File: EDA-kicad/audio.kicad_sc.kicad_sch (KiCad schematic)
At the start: 6 parts, among them J1 SJ2-35894B-SMT-TR, U7 CODEC-TLV320AIC3204IRHBR, U8 DAC-TLV320DAC3100IRHBR

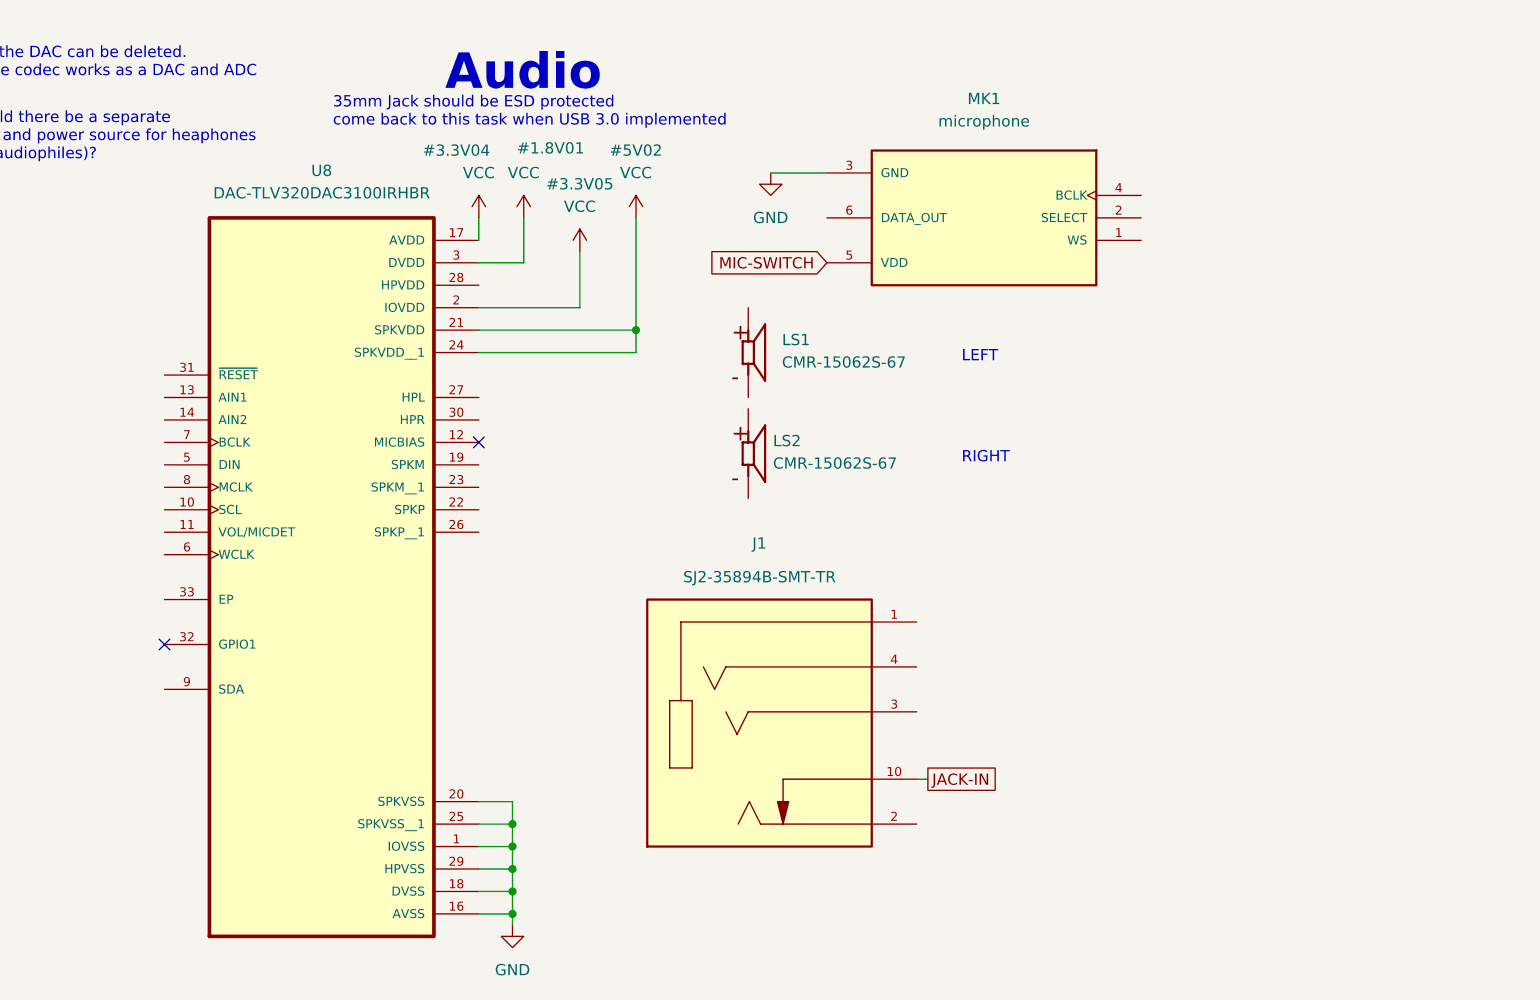
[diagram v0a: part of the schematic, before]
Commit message: add clearance
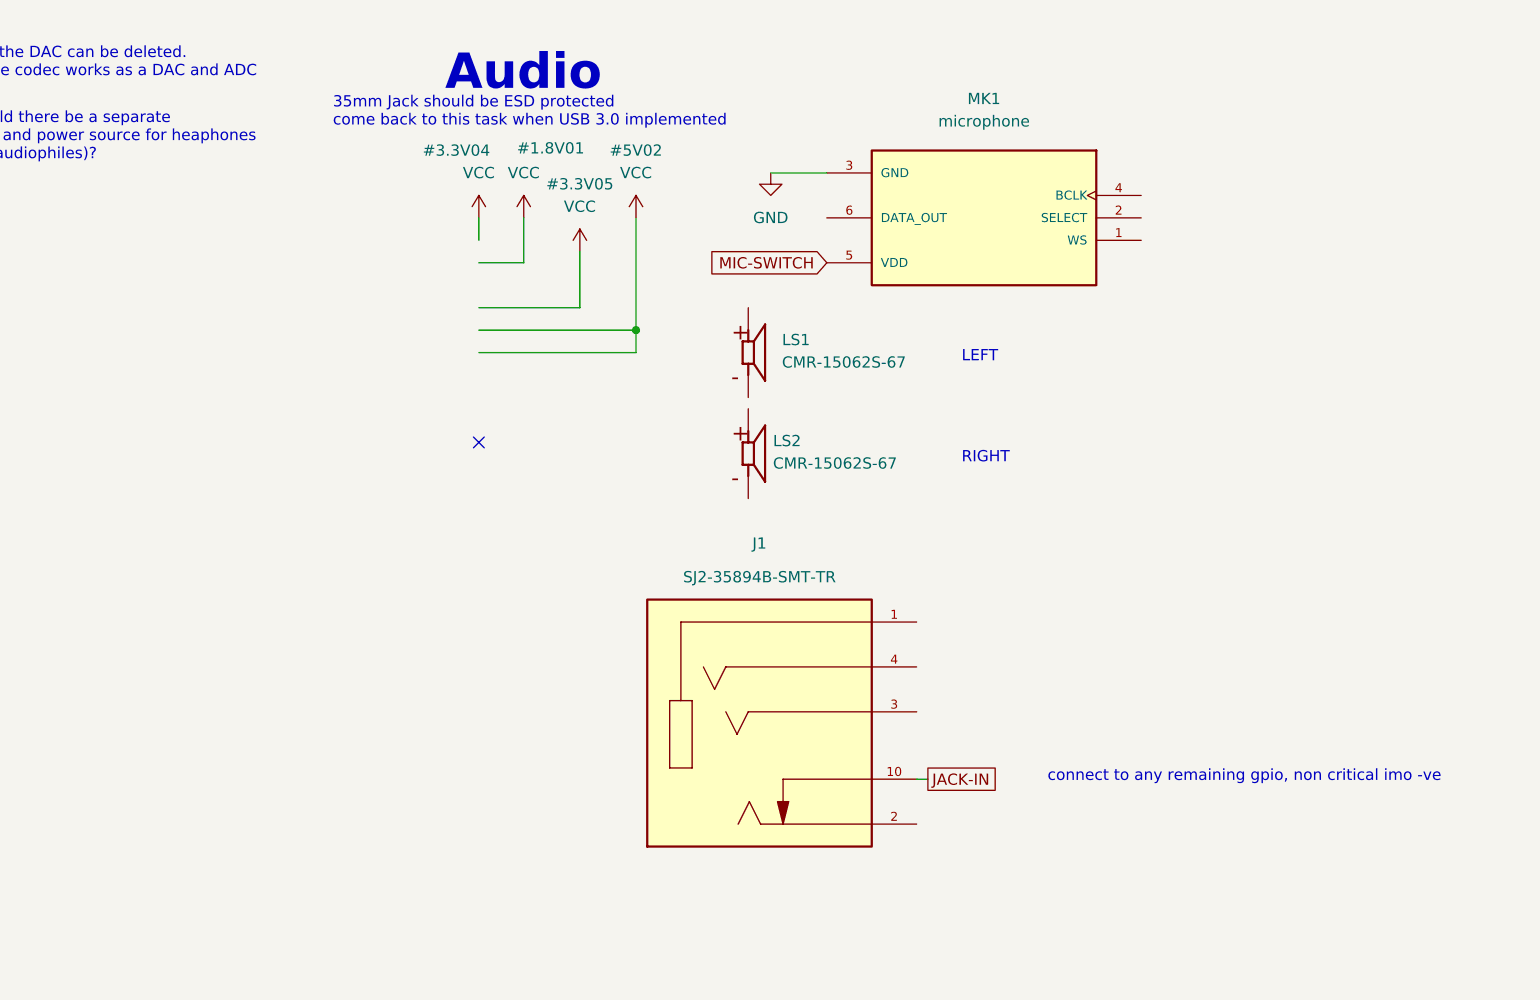
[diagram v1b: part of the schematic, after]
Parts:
- removed U8: DAC-TLV320DAC3100IRHBR, SPIRIT-footprints:DAC-IC_ADS125H01IRHBT, symbol SPIRIT-components:DAC-TLV320DAC3100IRHBR
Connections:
- no-connect marks 4 -> 3
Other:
- note added: "connect to any remaining gpio, non critical imo -ve"

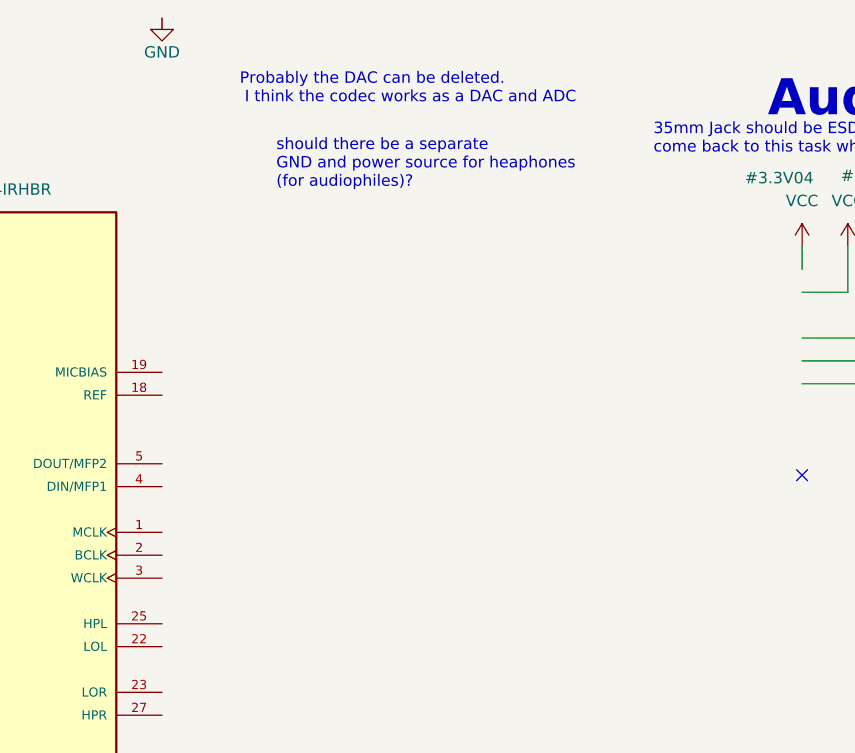
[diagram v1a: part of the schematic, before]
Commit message: connect codec clocks to GPIO and specify alt functions
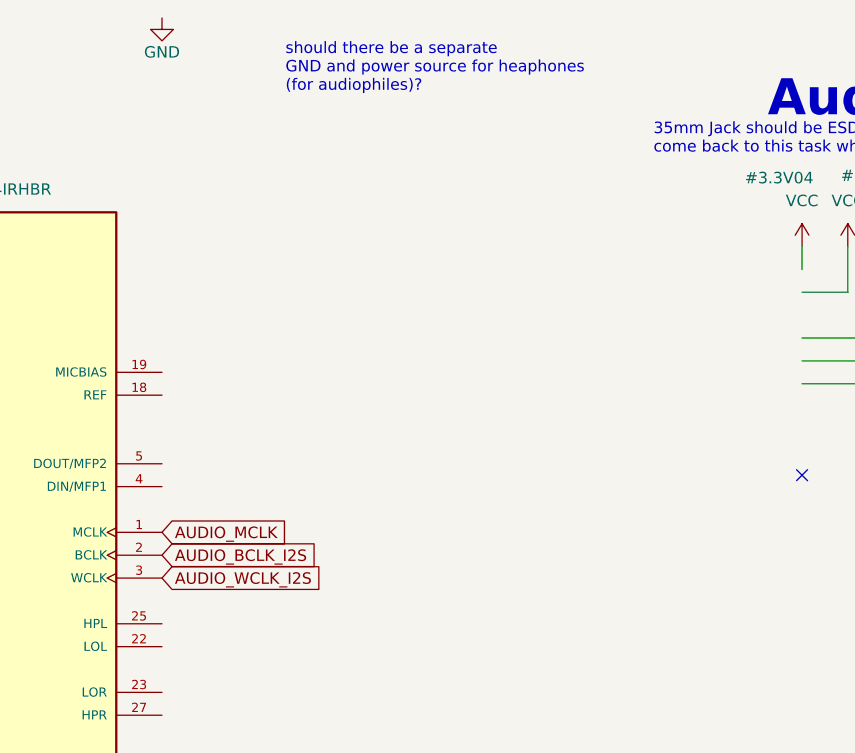
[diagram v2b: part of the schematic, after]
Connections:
- net AUDIO_MCLK: now reaches U7.1 (MCLK)
- net AUDIO_BCLK_I2S: now reaches U7.2 (BCLK)
- net AUDIO_WCLK_I2S: now reaches U7.3 (WCLK)
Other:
- note removed: "Probably the DAC can be deleted. I think the codec works as a DAC and ADC"
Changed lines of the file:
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@@
 	(text "should there be a separate \nGND and power source for heaphones\n(for audiophiles)?"
 		(exclude_from_sim no)
-		(at 118.11 58.42 0)
+		(at 119.126 47.752 0)
 		(effects
 			(font
@@
 		(exclude_from_sim no)
 		(at 231.14 81.28 0)
-		(effects
-			(font
-				(size 1.27 1.27)
-			)
-			(justify left bottom)
-		)
-	)
-	(text "Probably the DAC can be deleted.\n I think the codec works as a DAC and ADC"
-		(exclude_from_sim no)
-		(at 114.046 49.022 0)
 		(effects
 			(font
@@
 		)
 	)
+	(global_label "AUDIO_BCLK_I2S"
+		(shape input)
+		(at 105.41 99.06 0)
+		(fields_autoplaced yes)
+		(effects
+			(font
+				(size 1.27 1.27)
+			)
+			(justify left)
+		)
+		(property "Intersheetrefs" "${INTERSHEET_REFS}"
+			(at 123.8167 99.06 0)
+			(effects
+				(font
+					(size 1.27 1.27)
+				)
+				(justify left)
+				(hide yes)
+			)
+		)
+	)
 	(global_label "CODEC SCL"
 		(shape input)
@@
 				(hide yes)
 			)
+		)
+	)
+	(global_label "AUDIO_WCLK_I2S"
+		(shape input)
+		(at 105.41 101.6 0)
+		(fields_autoplaced yes)
+		(effects
+			(font
+				(size 1.27 1.27)
+			)
+			(justify left)
+		)
+		(property "Intersheetrefs" "${INTERSHEET_REFS}"
+			(at 123.9981 101.6 0)
+			(effects
+				(font
+					(size 1.27 1.27)
+				)
+				(justify left)
+				(hide yes)
+			)
+		)
+	)
+	(global_label "AUDIO_MCLK"
+		(shape input)
+		(at 105.41 96.52 0)
+		(fields_autoplaced yes)
+		(effects
+			(font
+				(size 1.27 1.27)
+			)
+			(justify left)
+		)
+		(property "Intersheetrefs" "${INTERSHEET_REFS}"
+			(at 120.0067 96.52 0)
+			(effects
+				(font
+					(size 1.27 1.27)
+				)
+				(justify left)
+				(hide yes)
+			)

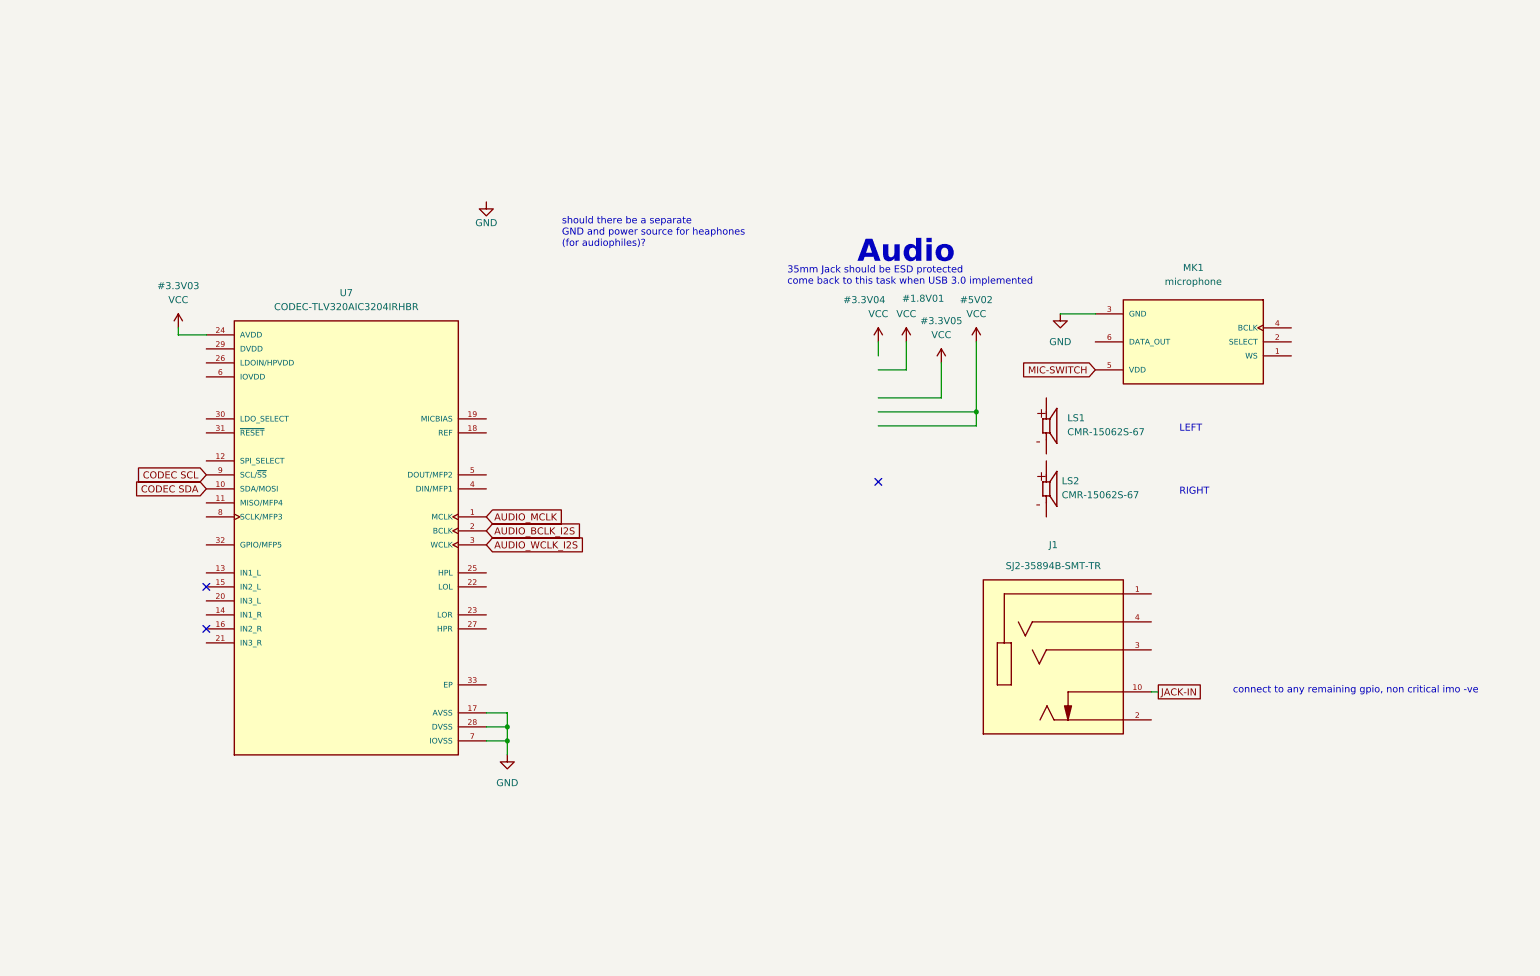
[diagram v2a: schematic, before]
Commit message: microhphone partially connected
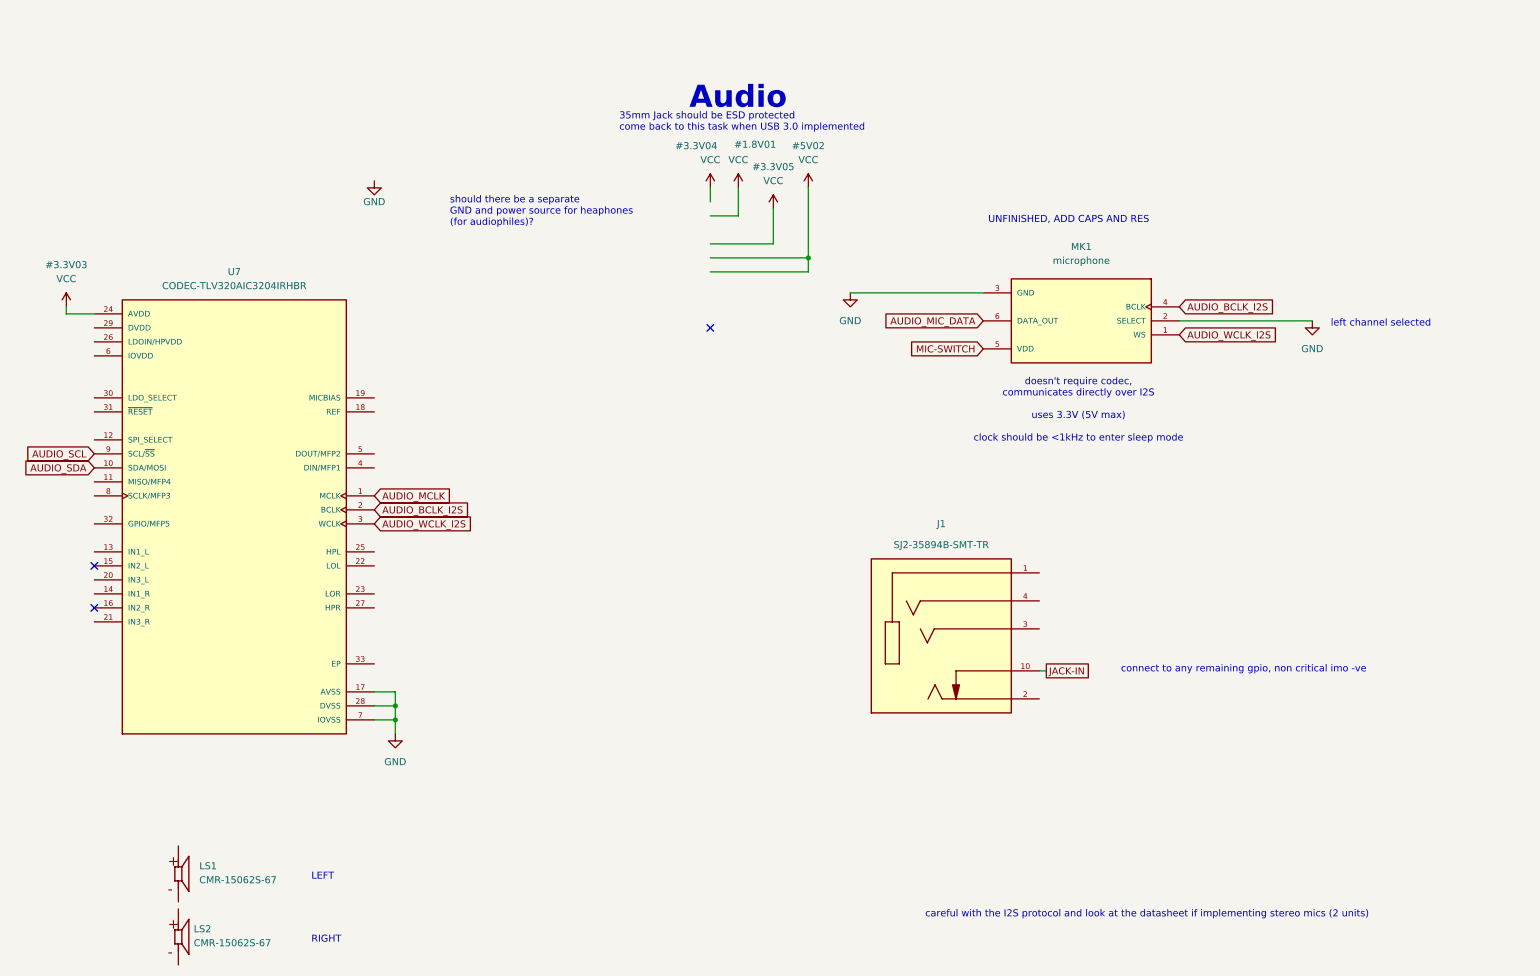
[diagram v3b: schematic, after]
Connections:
- net AUDIO_BCLK_I2S: now also MK1.4 (BCLK)
- net AUDIO_WCLK_I2S: now also MK1.1 (WS)
- net GND: now also MK1.2 (SELECT)
- net AUDIO_MIC_DATA: now reaches MK1.6 (DATA_OUT)
- net CODEC SCL renamed AUDIO_SCL
- net CODEC SDA renamed AUDIO_SDA
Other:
- note added: "UNFINISHED, ADD CAPS AND RES"
- note added: "careful with the I2S protocol and look at the datasheet if implementing stereo mics (2 units)"
- note added: "doesn't require codec, communicates directly over I2S uses 3.3V (5V max) clock should be <1kHz to enter sleep mode"
- note added: "left channel selected"
- moved on the sheet: J1, LS1, LS2, MK1, U7

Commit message: complete microphone schematic
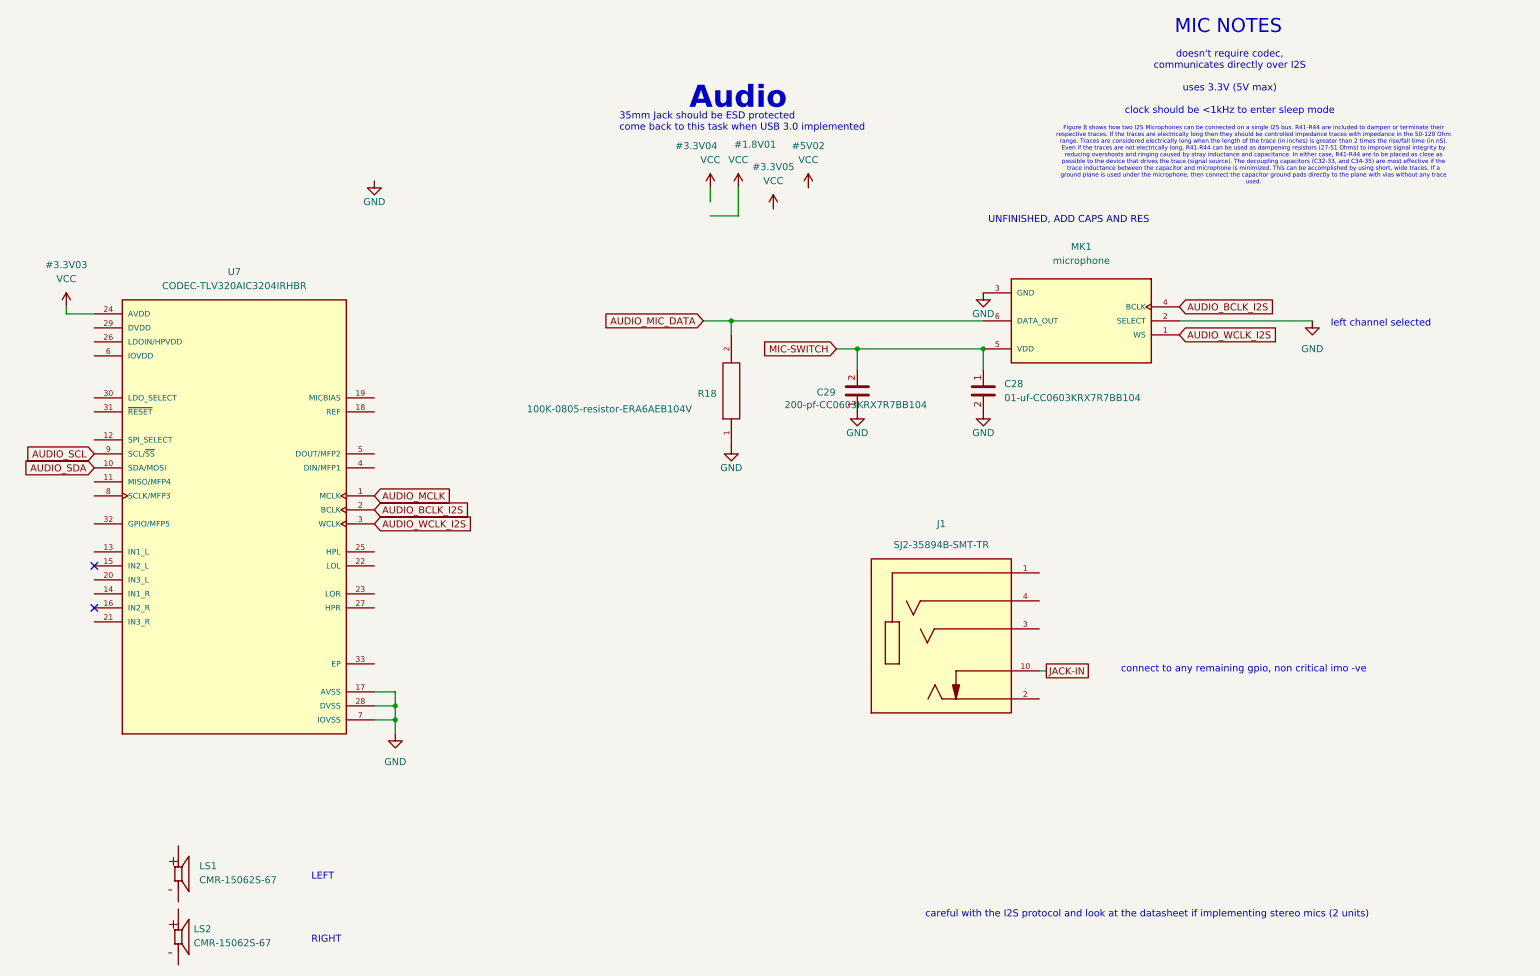
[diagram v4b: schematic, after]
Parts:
- added C28: 01-uf-CC0603KRX7R7BB104, CC0603KRX7R7BB104:CAPC1608X90, symbol SPIRIT-components:01-uf-CC0603KRX7R7BB104
- added C29: 200-pf-CC0603KRX7R7BB104, SPIRIT-footprints:0603-capacitor, symbol SPIRIT-components:200-pf-CC0603KRX7R7BB104
- added R18: 100K-0805-resistor-ERA6AEB104V, SPIRIT-footprints:100K-0805-resistor-RES_ERA6AEB104V, symbol SPIRIT-components:100K-0805-resistor-ERA6AEB104V
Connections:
- net AUDIO_MIC_DATA: now also R18.2
- net GND: now also C28.2, C29.1, R18.1
- net MIC-SWITCH: now also C28.1, C29.2
- no-connect marks 3 -> 2
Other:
- note added: "Figure 8 shows how two I2S Microphones can be connected on a single I2S bus. R41-R44 are included to dampen or terminate their respective traces. If the traces are electrically long then they should be controlled impedance traces with impedance in the 50-120 Ohm range. Traces are considered electrically long when the length of the trace (in inches) is greater than 2 times the rise/fall time (in n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"
- note added: "MIC NOTES"
- note removed: "should there be a separate GND and power source for heaphones (for audiophiles)?"
